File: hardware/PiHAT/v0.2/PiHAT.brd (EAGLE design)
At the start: 65 x 56.5 mm, 41 parts, among them U1 ATMEGA328P, U2 TSL2561, U3 OPA344, U4 MPL115A, U6 ADMP401, U7 SHT31-DIS, Y1 16MHZ

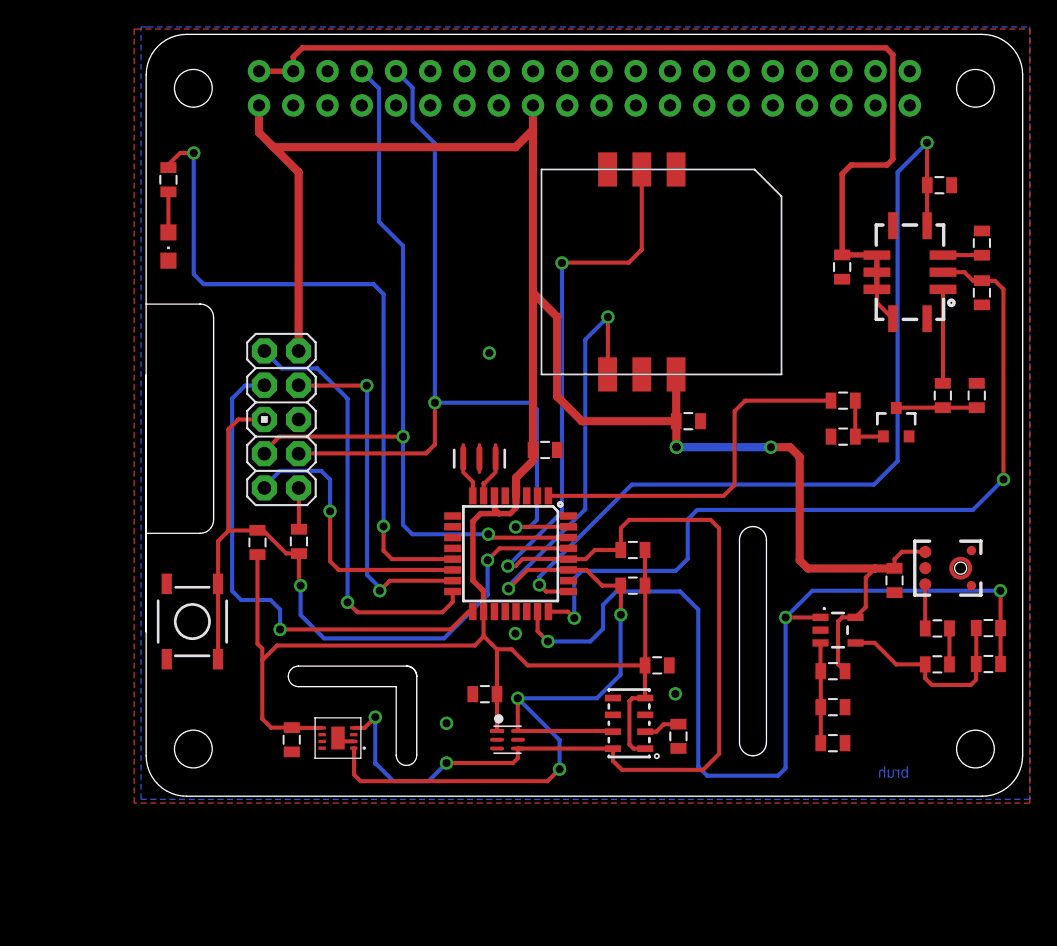
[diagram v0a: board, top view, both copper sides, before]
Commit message: Updated PiAQ HAT to v0.2
- Added LEDs on GPIO 05, 26
- Replaced IAQ Core with CCS811
- Added more thermal isolation and rerouted traces
- Minor silkscreen adjustments
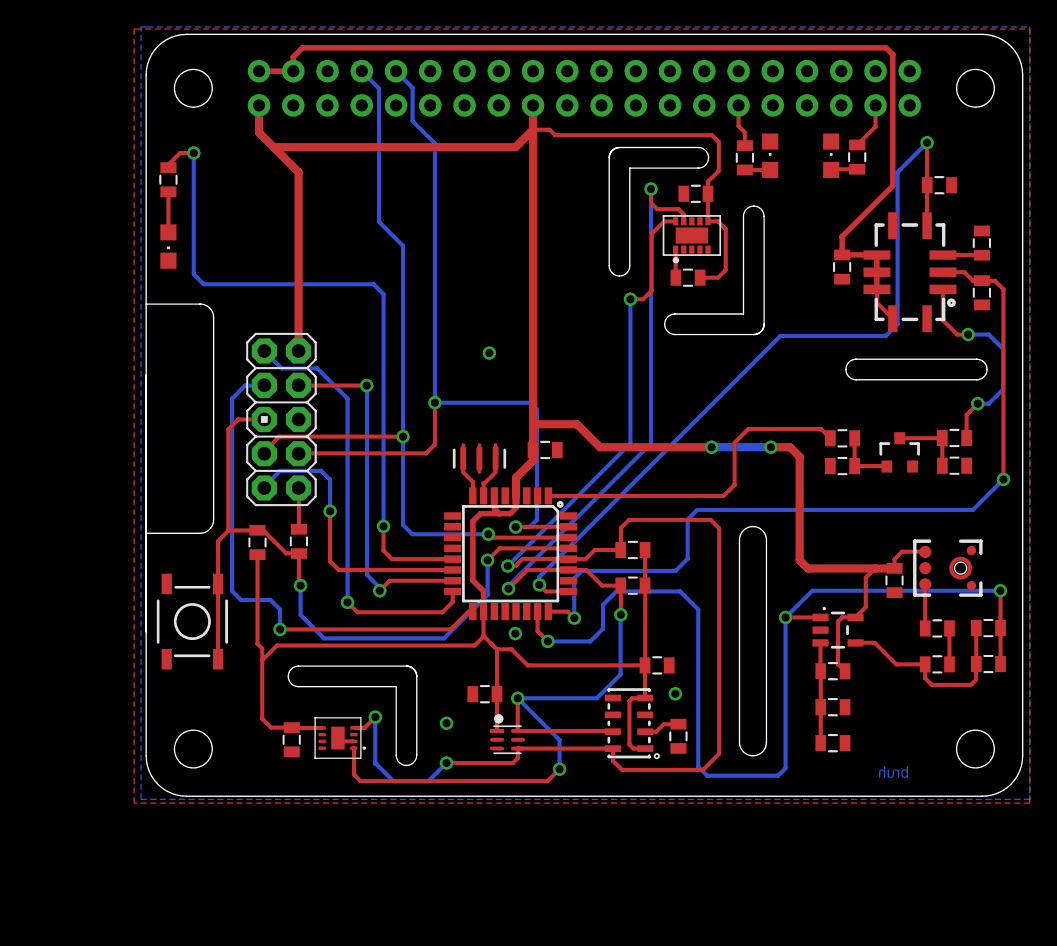
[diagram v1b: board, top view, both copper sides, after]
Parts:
- removed IAQ-CORE: IAQ-CORE, IAQ-CORE:IAQ-CORE
- added LED_05, LED_26: (no value), adafruit:CHIPLED_0805
- added R10, R2: 47, SparkFun-Resistors:0805
- added R9: 100K, SparkFun-Passives:0805
- added U$1: CCS811, CCS811:LGA
- moved C5 16.9 mm to (40.8, 43.4), turned to 180 degrees
- moved R17 5.46 mm to (59.9, 23.2), turned to 180 degrees
- moved R18 3.27 mm to (59.9, 25.3), turned to 0 degrees
- moved R20 2.79 mm to (51.6, 25.3)
- moved MOSFET 2.25 mm to (55.9, 24.2)
- moved R19 2.18 mm to (51.6, 23.2)
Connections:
- new net N$1: LED_26.A, R2.1
- new net N$16: R9.2, U$1.1
- new net N$6: LED_05.A, R10.1
- net GND: now also LED_05.C, LED_26.C, U$1.11; no longer IAQ-CORE.GND
- net GPIO26: now also R2.2
- net GPIO5: now also R10.2
- net SCL: now also U$1.10; no longer IAQ-CORE.SCL
- net SDA: now also U$1.9; no longer IAQ-CORE.SDA
- net VCC: now also R9.1, U$1.6; no longer IAQ-CORE.VCC
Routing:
- net VCC: track 214.0 -> 230.0 mm, vias 3 -> 2
- net SDA: track 85.6 -> 96.5 mm
- net N$8: track 6.98 -> 15.8 mm, vias 0 -> 2
- net VRED: track 63.7 -> 57.8 mm
- net SCL: track 106.0 -> 101.3 mm
- net GPIO26: track 0.00 -> 3.50 mm
- net GPIO5: track 0.00 -> 3.18 mm
- net N$16: track 0.00 -> 2.08 mm
- net PRE: track 27.1 -> 25.1 mm
- net N$1: track 0.00 -> 1.95 mm
- net N$6: track 0.00 -> 1.88 mm
- net 5V: track 74.3 -> 72.8 mm
- net N$20: track 5.98 -> 5.23 mm
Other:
- board text added: "Designed by Akram Ali"
- board text added: "v0.2"
- board text removed: "v0.1"

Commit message: Minor fixes to sensor board v0.6
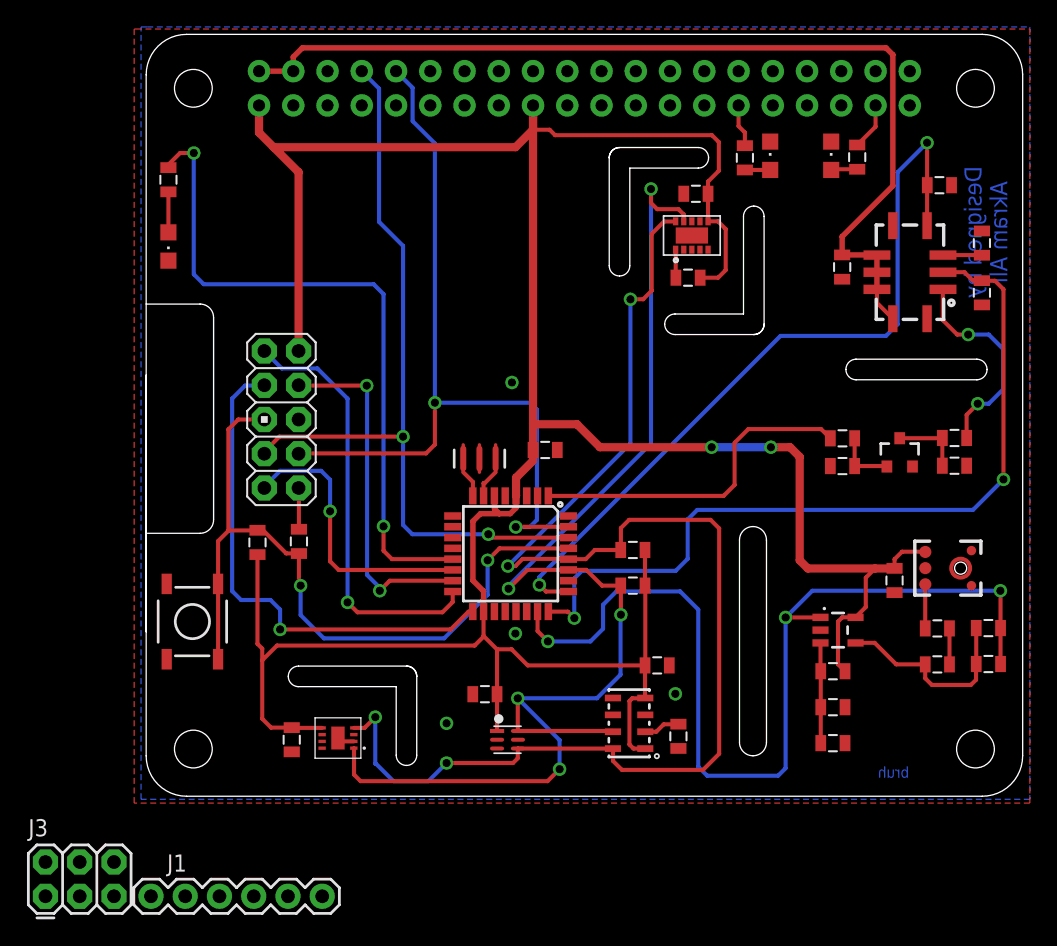
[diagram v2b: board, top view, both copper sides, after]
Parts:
- added J1: FTDI_BASICPTH, SparkFun-Connectors:FTDI_BASIC
- added J3: AVR_SPI_PRG_6PTH, SparkFun-Connectors:2X3
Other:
- board text added: "piaq.io"
- board text removed: "crtlabs.org"
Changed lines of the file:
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@@
 <layer number="118" name="Rect_Pads" color="7" fill="1" visible="no" active="yes"/>
 <layer number="121" name="sName" color="7" fill="1" visible="yes" active="yes"/>
-<layer number="122" name="_bPlace" color="7" fill="1" visible="no" active="yes"/>
+<layer number="122" name="_bPlace" color="7" fill="1" visible="yes" active="yes"/>
 <layer number="123" name="tTestmark" color="7" fill="1" visible="no" active="yes"/>
 <layer number="124" name="bTestmark" color="7" fill="1" visible="no" active="yes"/>
@@
 <rectangle x1="13.65885" y1="45.72635" x2="14.11605" y2="45.76445" layer="121"/>
 <text x="25.2476" y="33.3248" size="1.27" layer="121" font="vector" align="bottom-center">v0.2</text>
-<text x="51.943" y="-0.2032" size="1.27" layer="121" font="vector" ratio="13" align="bottom-center">crtlabs.org</text>
+<text x="23.7998" y="31.4452" size="1.27" layer="121" font="vector" ratio="13" align="bottom-center">piaq.io</text>
 <rectangle x1="18.923" y1="35.0266" x2="18.9738" y2="35.0774" layer="121"/>
 <rectangle x1="19.0246" y1="35.0266" x2="19.0754" y2="35.0774" layer="121"/>
@@
 <rectangle x1="13.8938" y1="39.0398" x2="14.2494" y2="39.0906" layer="121"/>
 <rectangle x1="13.9446" y1="39.0906" x2="14.1986" y2="39.1414" layer="121"/>
-<text x="55.4228" y="0.1016" size="0.8128" layer="16" font="vector" rot="MR0" align="bottom-center">bruh</text>
-<text x="63.9572" y="39.497" size="1.27" layer="122" font="vector" rot="SMR270" align="bottom-center">Designed by
+<text x="55.4228" y="0.1016" size="0.8128" layer="16" font="vector" ratio="12" rot="MR0" align="bottom-center">bruh</text>
+<text x="63.8556" y="40.5638" size="1.27" layer="16" font="vector" ratio="12" rot="SMR270" align="bottom-center">Designed by
 Akram Ali</text>
 <wire x1="45.8216" y1="41.7322" x2="45.0596" y2="42.4942" width="0.0254" layer="20" curve="90"/>
@@
 <attribute name="VALUE" x="48.8188" y="44.958" size="1.27" layer="27" rot="R90"/>
 </element>
+<element name="J1" library="SparkFun-Connectors" package="FTDI_BASIC" value="FTDI_BASICPTH" x="0.3556" y="-8.6868"/>
+<element name="J3" library="SparkFun-Connectors" package="2X3" value="AVR_SPI_PRG_6PTH" x="-7.4676" y="-8.6868"/>
 </elements>
 <signals>
@@
 <via x="27.3812" y="10.795" extent="1-16" drill="0.6"/>
 <via x="39.243" y="6.3246" extent="1-16" drill="0.6"/>
-<via x="25.4508" y="31.5976" extent="1-16" drill="0.6"/>
+<via x="27.1272" y="29.4132" extent="1-16" drill="0.6"/>
 <contactref element="LED_26" pad="C"/>
 <contactref element="U$1" pad="11"/>

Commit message: Added FTDI headers to Pi HAT, separated ISP headers
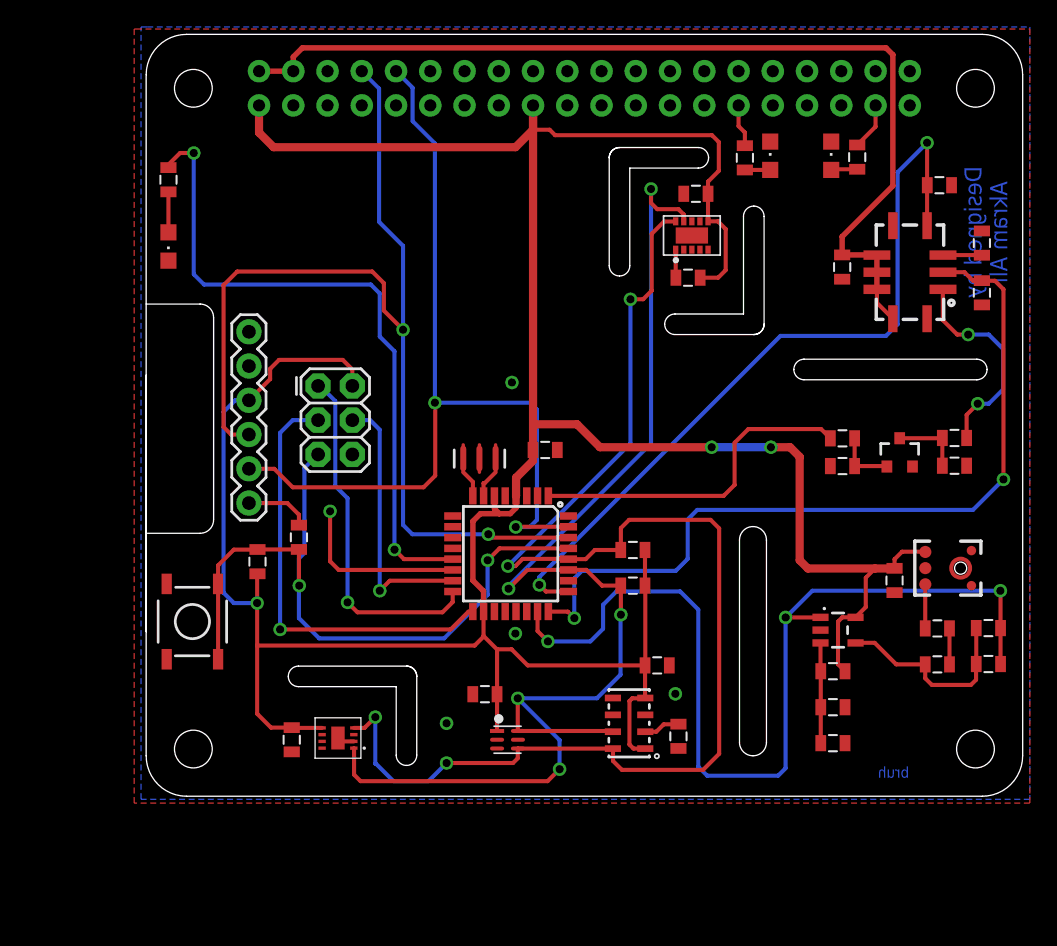
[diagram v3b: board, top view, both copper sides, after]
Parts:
- removed J2: (no value), SparkFun-Connectors:AVR_ICSP
- J1: value FTDI_BASICPTH -> FTDI
- J3: value AVR_SPI_PRG_6PTH -> ISP
- moved J3 42.9 mm to (12.8, 29.2), turned to 270 degrees
- moved J1 30.1 mm to (7.62, 20.5), turned to 90 degrees
- moved R13 1.42 mm to (8.26, 16.1)
- moved C12 0.30 mm to (11.3, 17.9)
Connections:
- net DTR: now also J1.DTR; no longer J2.10
- net GND: now also J1.CTS, J1.GND, J3.6; no longer J2.6
- net MISO: now also J3.1; no longer J2.1
- net MOSI: now also J3.4; no longer J2.4
- net RESET: now also J3.5; no longer J2.5
- net RX: now also J1.TXO; no longer J2.7
- net SCK: now also J3.3; no longer J2.3
- net SS: no longer J2.9
- net TX: now also J1.RXI; no longer J2.8
- net VCC: now also J1.VCC, J3.2; no longer J2.2
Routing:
- net RX: track 58.5 -> 76.9 mm
- net VCC: track 230.0 -> 242.0 mm, vias 2 -> 3
- net SS: track 21.1 -> 13.1 mm
- net TX: track 60.9 -> 67.6 mm
- net MOSI: track 26.4 -> 20.0 mm, vias 2 -> 1
- net MISO: track 31.9 -> 26.2 mm
- net SCK: track 37.5 -> 32.6 mm
- net RESET: track 55.8 -> 53.8 mm
- net DTR: track 3.07 -> 4.84 mm
- net N$2: track 50.6 -> 50.0 mm
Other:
- board text removed: "DTR"
- board text removed: "ISP"
- board text removed: "SS"
